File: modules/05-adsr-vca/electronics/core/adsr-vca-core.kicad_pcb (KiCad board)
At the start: 2 copper layers, 58 x 65 mm, 67 parts, among them J2 Conn_02x03_Odd_Even, J3 Conn_02x03_Odd_Even, J4 Conn_02x06_Odd_Even, J5 Conn_02x03_Odd_Even, J6 Conn_01x02, J7 Conn_02x05_Odd_Even, J8 Conn_02x03_Odd_Even, Q1 BC857, Q3 BC847BS, U1 LM324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

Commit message: ADSR+VCA JLCPCB verified for v1.0
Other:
- board text added: "SHMØERGH MODULEUR"
- board text added: "SM-05 ADSR VCA V1.0 / 2025 DEC"
- board text removed: "HM-05 ADSR VCA V0.2 / 2025 Aug"
- board text removed: "SHMØERGH HOG MODULEUR"

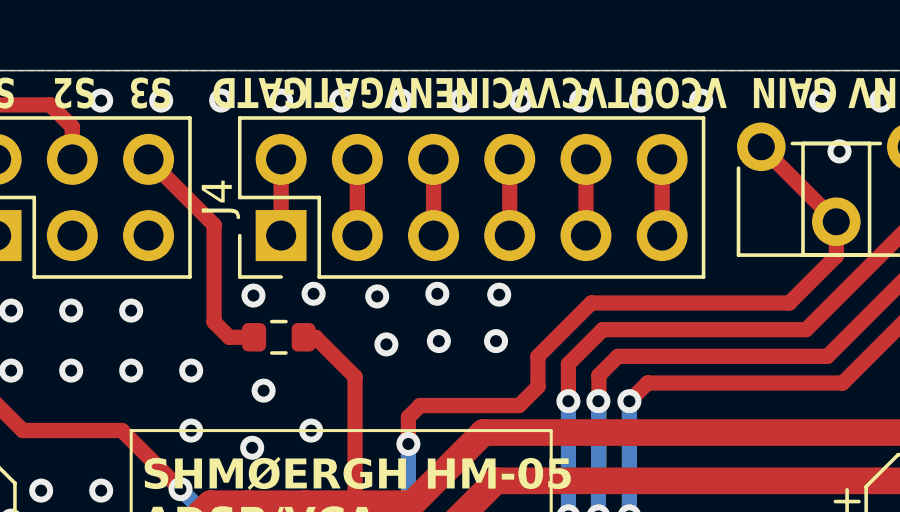
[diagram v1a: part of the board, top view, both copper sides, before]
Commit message: Fixed ADSR default connector
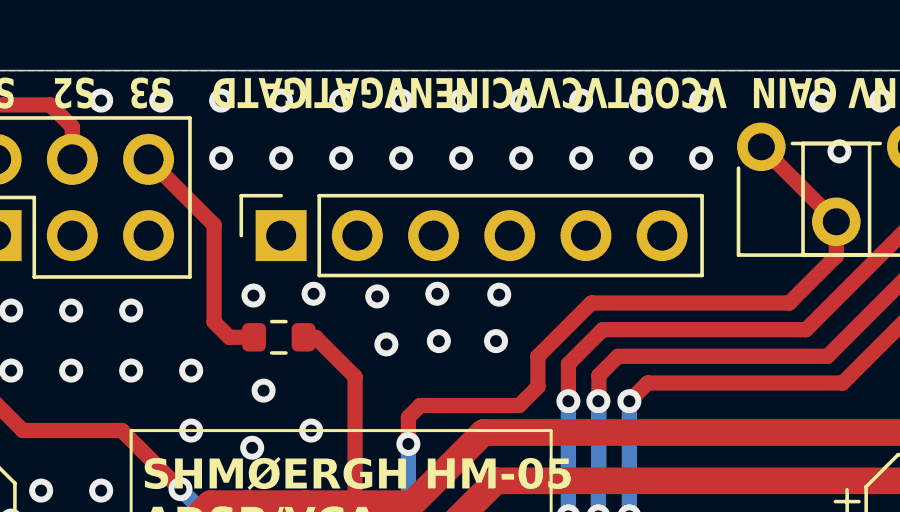
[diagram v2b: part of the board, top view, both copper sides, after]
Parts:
- J4: value Conn_02x06_Odd_Even -> Conn_01x06; footprint Connector_PinHeader_2.54mm:PinHeader_2x06_P2.54mm_Vertical -> Connector_PinSocket_2.54mm:PinSocket_1x06_P2.54mm_Vertical
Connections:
- J4 pad 1: Net-(J4-Pin_1) -> unconnected-(J4-Pin_1-Pad1)
- J4 pad 2: Net-(J4-Pin_1) -> unconnected-(J4-Pin_2-Pad2)
- J4 pad 3: Net-(J4-Pin_3) -> unconnected-(J4-Pin_3-Pad3)
- J4 pad 4: Net-(J4-Pin_3) -> unconnected-(J4-Pin_4-Pad4)
- J4 pad 5: Net-(J4-Pin_5) -> unconnected-(J4-Pin_5-Pad5)
- J4 pad 6: Net-(J4-Pin_5) -> unconnected-(J4-Pin_6-Pad6)
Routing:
- net Net-(J4-Pin_7): track 2.54 -> 0.00 mm
- net Net-(J4-Pin_5): track 2.54 -> 0.00 mm
- net Net-(J4-Pin_3): track 2.54 -> 0.00 mm
- net Net-(J4-Pin_11): track 2.54 -> 0.00 mm
- net Net-(J4-Pin_10): track 2.54 -> 0.00 mm
- net Net-(J4-Pin_1): track 2.54 -> 0.00 mm
- net GND: vias 330 -> 339
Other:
- board text added: "DEFAULTS"

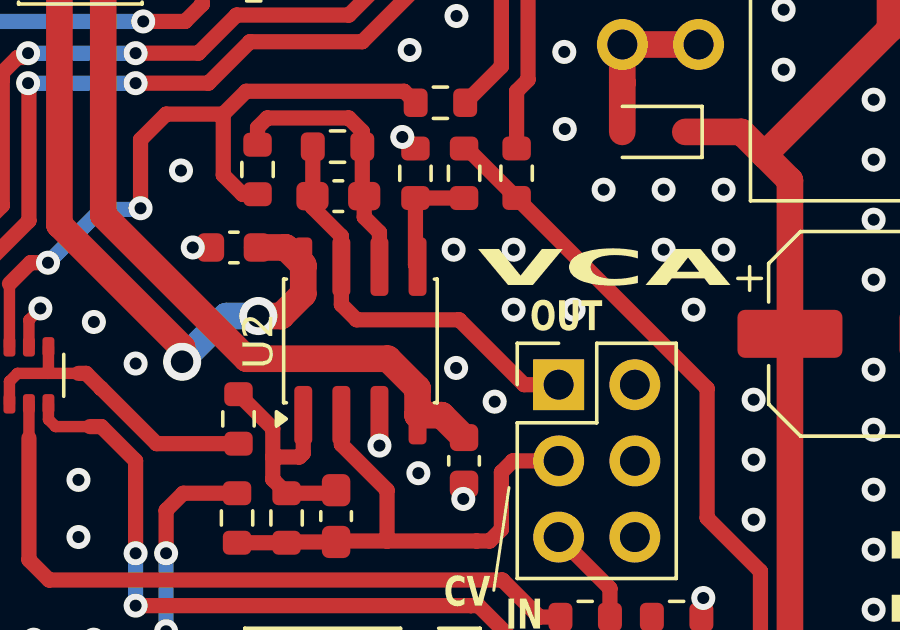
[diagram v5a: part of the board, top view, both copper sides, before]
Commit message: Added output resistor for VCA
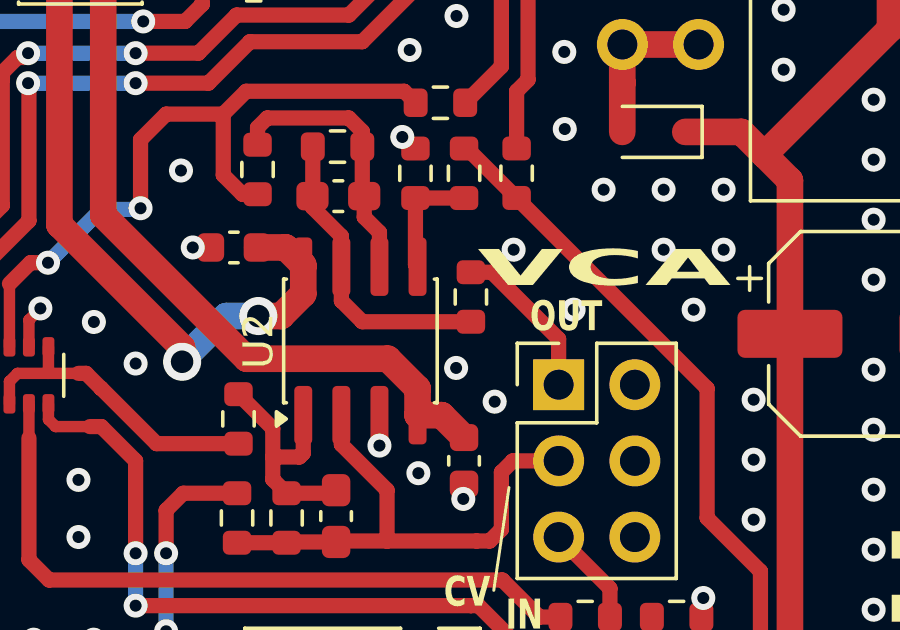
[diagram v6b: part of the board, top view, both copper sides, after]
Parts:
- added R15: 1k, Resistor_SMD:R_0603_1608Metric, F.Cu at (152.6, 88.6)
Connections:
- C8 pad 2: VCA_OUT -> Net-(C8-Pad2)
- R28 pad 2: VCA_OUT -> Net-(C8-Pad2)
- U2 pad 7: VCA_OUT -> Net-(C8-Pad2)
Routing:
- net Net-(C8-Pad2): track 0.00 -> 10.2 mm
- net VCA_OUT: track 14.0 -> 5.37 mm
- net GND: vias 339 -> 337

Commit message: Bumped rev of ADSR+VCA core board
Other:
- board text added: "SHMØERGH HM-05 ADSR/VCA core v1.2 2026 FEB"
- board text removed: "SHMØERGH HM-05 ADSR/VCA core v0.2 2025.OCT"
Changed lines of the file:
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@@
 		)
 	)
-	(gr_text "SHMØERGH HM-05 \nADSR/VCA core\nv0.2 2025.OCT"
+	(gr_text "SHMØERGH HM-05 \nADSR/VCA core\nv1.2 2026 FEB"
 		(at 138.351 61.272 0)
 		(layer "F.SilkS")
@@
 			(justify left bottom)
 		)
-		(render_cache "SHMØERGH HM-05 \nADSR/VCA core\nv0.2 2025.OCT" 0
+		(render_cache "SHMØERGH HM-05 \nADSR/VCA core\nv1.2 2026 FEB" 0
 			(polygon
 				(pts
@@
 			(polygon
 				(pts
-					(xy 139.368271 60.207216) (xy 139.368271 60.974749) (xy 139.499429 60.974749) (xy 139.499429 60.720187)
-					(xy 139.626741 60.720187) (xy 139.626741 60.589028) (xy 139.499429 60.589028) (xy 139.499429 60.207216)
-				)
-			)
-			(polygon
-				(pts
-					(xy 139.495521 60.970841) (xy 139.495521 61.102) (xy 139.881242 61.102) (xy 139.881242 60.970841)
-				)
-			)
-			(polygon
-				(pts
-					(xy 139.495521 60.079904) (xy 139.495521 60.211124) (xy 139.881242 60.211124) (xy 139.881242 60.079904)
-				)
-			)
-			(polygon
-				(pts
-					(xy 139.877334 60.207216) (xy 139.877334 60.334466) (xy 139.750084 60.334466) (xy 139.750084 60.465686)
-					(xy 139.877334 60.465686) (xy 139.877334 60.974749) (xy 140.008554 60.974749) (xy 140.008554 60.207216)
-				)
-			)
-			(polygon
-				(pts
-					(xy 139.622833 60.461778) (xy 139.622833 60.592936) (xy 139.753991 60.592936) (xy 139.753991 60.461778)
+					(xy 139.622833 60.338374) (xy 139.622833 60.970841) (xy 139.368271 60.970841) (xy 139.368271 61.102)
+					(xy 140.008554 61.102) (xy 140.008554 60.970841) (xy 139.753991 60.970841) (xy 139.753991 60.079904)
+					(xy 139.622833 60.079904) (xy 139.622833 60.207216) (xy 139.368271 60.207216) (xy 139.368271 60.338374)
 				)
 			)
@@
 			(polygon
 				(pts
-					(xy 145.598418 60.079904) (xy 145.598418 60.592936) (xy 146.111389 60.592936) (xy 146.111389 60.461778)
-					(xy 145.729576 60.461778) (xy 145.729576 60.211124) (xy 146.2387 60.211124) (xy 146.2387 60.079904)
+					(xy 145.725668 60.079904) (xy 145.725668 60.211124) (xy 146.111389 60.211124) (xy 146.111389 60.079904)
+				)
+			)
+			(polygon
+				(pts
+					(xy 145.598418 60.207216) (xy 145.598418 60.974749) (xy 145.729576 60.974749) (xy 145.729576 60.592936)
+					(xy 146.111389 60.592936) (xy 146.111389 60.461778) (xy 145.729576 60.461778) (xy 145.729576 60.207216)
 				)
 			)
@@
 			(polygon
 				(pts
-					(xy 146.111389 60.970841) (xy 145.725668 60.970841) (xy 145.725668 61.102) (xy 146.111389 61.102)
-				)
-			)
-			(polygon
-				(pts
-					(xy 145.729576 60.974749) (xy 145.729576 60.843591) (xy 145.598418 60.843591) (xy 145.598418 60.974749)
-				)
-			)
-			(polygon
-				(pts
-					(xy 146.743001 60.843591) (xy 146.743001 61.102) (xy 146.874159 61.102) (xy 146.874159 60.843591)
-				)
-			)
-			(polygon
-				(pts
-					(xy 147.378459 60.207216) (xy 147.378459 60.974749) (xy 147.509618 60.974749) (xy 147.509618 60.207216)
-				)
-			)
-			(polygon
-				(pts
-					(xy 147.50571 60.970841) (xy 147.50571 61.102) (xy 147.89143 61.102) (xy 147.89143 60.970841)
-				)
-			)
-			(polygon
-				(pts
-					(xy 147.887523 60.207216) (xy 147.887523 60.974749) (xy 148.018742 60.974749) (xy 148.018742 60.207216)
-				)
-			)
-			(polygon
-				(pts
-					(xy 147.50571 60.079904) (xy 147.50571 60.211124) (xy 147.89143 60.211124) (xy 147.89143 60.079904)
-				)
-			)
-			(polygon
-				(pts
-					(xy 148.26848 60.207216) (xy 148.26848 60.974749) (xy 148.399639 60.974749) (xy 148.399639 60.207216)
-				)
-			)
-			(polygon
-				(pts
-					(xy 148.395731 60.970841) (xy 148.395731 61.102) (xy 148.781451 61.102) (xy 148.781451 60.970841)
-				)
-			)
-			(polygon
-				(pts
-					(xy 148.777543 60.843591) (xy 148.777543 60.974749) (xy 148.908763 60.974749) (xy 148.908763 60.843591)
-				)
-			)
-			(polygon
-				(pts
-					(xy 148.395731 60.079904) (xy 148.395731 60.211124) (xy 148.781451 60.211124) (xy 148.781451 60.079904)
-				)
-			)
-			(polygon
-				(pts
-					(xy 148.777543 60.207216) (xy 148.777543 60.338374) (xy 148.908763 60.338374) (xy 148.908763 60.207216)
-				)
-			)
-			(polygon
-				(pts
-					(xy 149.158501 60.079904) (xy 149.158501 60.211124) (xy 149.413063 60.211124) (xy 149.413063 61.102)
-					(xy 149.544222 61.102) (xy 149.544222 60.211124) (xy 149.798784 60.211124) (xy 149.798784 60.079904)
-				)
-			)
+					(xy 145.725668 60.970841) (xy 145.725668 61.102) (xy 146.111389 61.102) (xy 146.111389 60.970841)
+				)
+			)
+			(polygon
+				(pts
+					(xy 146.107481 60.207216) (xy 146.107481 60.338374) (xy 146.2387 60.338374) (xy 146.2387 60.207216)
+				)
+			)
+			(polygon
+				(pts
+					(xy 147.378459 60.079904) (xy 147.378459 61.102) (xy 147.509618 61.102) (xy 147.509618 60.592936)
+					(xy 147.89143 60.592936) (xy 147.89143 60.461778) (xy 147.509618 60.461778) (xy 147.509618 60.211124)
+					(xy 148.018742 60.211124) (xy 148.018742 60.079904)
+				)
+			)
+			(polygon
+				(pts
+					(xy 148.26848 60.079904) (xy 148.26848 61.102) (xy 148.908763 61.102) (xy 148.908763 60.970841)
+					(xy 148.399639 60.970841) (xy 148.399639 60.592936) (xy 148.781451 60.592936) (xy 148.781451 60.461778)
+					(xy 148.399639 60.461778) (xy 148.399639 60.211124) (xy 148.908763 60.211124) (xy 148.908763 60.079904)
+				)
+			)
+			(polygon
+				(pts
+					(xy 149.158501 60.079904) (xy 149.158501 61.102) (xy 149.671472 61.102) (xy 149.671472 60.970841)
+					(xy 149.28966 60.970841) (xy 149.28966 60.592936) (xy 149.671472 60.592936) (xy 149.671472 60.461778)
+					(xy 149.28966 60.461778) (xy 149.28966 60.211124) (xy 149.671472 60.211124) (xy 149.671472 60.079904)
+				)
+			)
+			(polygon
+				(pts
+					(xy 149.667564 60.589028) (xy 149.667564 60.974749) (xy 149.798784 60.974749) (xy 149.798784 60.589028)
+				)
+			)
+			(polygon
+				(pts
+					(xy 149.667564 60.207216) (xy 149.667564 60.465686) (xy 149.798784 60.465686) (xy 149.798784 60.207216)
+				)
+			)

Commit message: KiCAD version update - ADSR+VCA
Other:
- board text added: "SHMØERGH HM-05 ADSR/VCA core v1.2"
- board text removed: "SHMØERGH HM-05 ADSR/VCA core v1.2 2026 FEB"
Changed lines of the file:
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@@
 		)
 	)
-	(gr_text "SHMØERGH HM-05 \nADSR/VCA core\nv1.2 2026 FEB"
+	(gr_text "SHMØERGH HM-05 \nADSR/VCA core\nv1.2"
 		(at 138.351 61.272 0)
 		(layer "F.SilkS")
@@
 			(justify left bottom)
 		)
-		(render_cache "SHMØERGH HM-05 \nADSR/VCA core\nv1.2 2026 FEB" 0
+		(render_cache "SHMØERGH HM-05 \nADSR/VCA core\nv1.2" 0
 			(polygon
 				(pts
@@
 				)
 			)
-			(polygon
-				(pts
-					(xy 142.928355 60.843591) (xy 142.928355 61.102) (xy 143.568637 61.102) (xy 143.568637 60.970841)
-					(xy 143.059513 60.970841) (xy 143.059513 60.843591)
-				)
-			)
-			(polygon
-				(pts
-					(xy 143.441326 60.211124) (xy 143.441326 60.079904) (xy 143.055605 60.079904) (xy 143.055605 60.211124)
-				)
-			)
-			(polygon
-				(pts
-					(xy 143.437418 60.207216) (xy 143.437418 60.465686) (xy 143.568637 60.465686) (xy 143.568637 60.207216)
-				)
-			)
-			(polygon
-				(pts
-					(xy 143.055605 60.716279) (xy 143.055605 60.847498) (xy 143.186825 60.847498) (xy 143.186825 60.716279)
-				)
-			)
-			(polygon
-				(pts
-					(xy 142.928355 60.207216) (xy 142.928355 60.338374) (xy 143.059513 60.338374) (xy 143.059513 60.207216)
-				)
-			)
-			(polygon
-				(pts
-					(xy 143.310167 60.461778) (xy 143.310167 60.592936) (xy 143.441326 60.592936) (xy 143.441326 60.461778)
-				)
-			)
-			(polygon
-				(pts
-					(xy 143.182917 60.589028) (xy 143.182917 60.720187) (xy 143.314075 60.720187) (xy 143.314075 60.589028)
-				)
-			)
-			(polygon
-				(pts
-					(xy 143.818376 60.207216) (xy 143.818376 60.974749) (xy 143.949534 60.974749) (xy 143.949534 60.720187)
-					(xy 144.076846 60.720187) (xy 144.076846 60.589028) (xy 143.949534 60.589028) (xy 143.949534 60.207216)
-				)
-			)
-			(polygon
-				(pts
-					(xy 143.945626 60.970841) (xy 143.945626 61.102) (xy 144.331347 61.102) (xy 144.331347 60.970841)
-				)
-			)
-			(polygon
-				(pts
-					(xy 143.945626 60.079904) (xy 143.945626 60.211124) (xy 144.331347 60.211124) (xy 144.331347 60.079904)
-				)
-			)
-			(polygon
-				(pts
-					(xy 144.327439 60.207216) (xy 144.327439 60.334466) (xy 144.200188 60.334466) (xy 144.200188 60.465686)
-					(xy 144.327439 60.465686) (xy 144.327439 60.974749) (xy 144.458658 60.974749) (xy 144.458658 60.207216)
-				)
-			)
-			(polygon
-				(pts
-					(xy 144.072938 60.461778) (xy 144.072938 60.592936) (xy 144.204096 60.592936) (xy 144.204096 60.461778)
-				)
-			)
-			(polygon
-				(pts
-					(xy 144.708397 60.843591) (xy 144.708397 61.102) (xy 145.348679 61.102) (xy 145.348679 60.970841)
-					(xy 144.839555 60.970841) (xy 144.839555 60.843591)
-				)
-			)
-			(polygon
-				(pts
-					(xy 145.221368 60.211124) (xy 145.221368 60.079904) (xy 144.835647 60.079904) (xy 144.835647 60.211124)
-				)
-			)
-			(polygon
-				(pts
-					(xy 145.21746 60.207216) (xy 145.21746 60.465686) (xy 145.348679 60.465686) (xy 145.348679 60.207216)
-				)
-			)
-			(polygon
-				(pts
-					(xy 144.835647 60.716279) (xy 144.835647 60.847498) (xy 144.966867 60.847498) (xy 144.966867 60.716279)
-				)
-			)
-			(polygon
-				(pts
-					(xy 144.708397 60.207216) (xy 144.708397 60.338374) (xy 144.839555 60.338374) (xy 144.839555 60.207216)
-				)
-			)
-			(polygon
-				(pts
-					(xy 145.090209 60.461778) (xy 145.090209 60.592936) (xy 145.221368 60.592936) (xy 145.221368 60.461778)
-				)
-			)
-			(polygon
-				(pts
-					(xy 144.962959 60.589028) (xy 144.962959 60.720187) (xy 145.094117 60.720187) (xy 145.094117 60.589028)
-				)
-			)
-			(polygon
-				(pts
-					(xy 145.725668 60.079904) (xy 145.725668 60.211124) (xy 146.111389 60.211124) (xy 146.111389 60.079904)
-				)
-			)
-			(polygon
-				(pts
-					(xy 145.598418 60.207216) (xy 145.598418 60.974749) (xy 145.729576 60.974749) (xy 145.729576 60.592936)
-					(xy 146.111389 60.592936) (xy 146.111389 60.461778) (xy 145.729576 60.461778) (xy 145.729576 60.207216)
-				)
-			)
-			(polygon
-				(pts
-					(xy 146.107481 60.589028) (xy 146.107481 60.974749) (xy 146.2387 60.974749) (xy 146.2387 60.589028)
-				)
-			)
-			(polygon
-				(pts
-					(xy 145.725668 60.970841) (xy 145.725668 61.102) (xy 146.111389 61.102) (xy 146.111389 60.970841)
-				)
-			)
-			(polygon
-				(pts
-					(xy 146.107481 60.207216) (xy 146.107481 60.338374) (xy 146.2387 60.338374) (xy 146.2387 60.207216)
-				)
-			)
-			(polygon
-				(pts
-					(xy 147.378459 60.079904) (xy 147.378459 61.102) (xy 147.509618 61.102) (xy 147.509618 60.592936)
-					(xy 147.89143 60.592936) (xy 147.89143 60.461778) (xy 147.509618 60.461778) (xy 147.509618 60.211124)
-					(xy 148.018742 60.211124) (xy 148.018742 60.079904)
-				)
-			)
-			(polygon
-				(pts
-					(xy 148.26848 60.079904) (xy 148.26848 61.102) (xy 148.908763 61.102) (xy 148.908763 60.970841)
-					(xy 148.399639 60.970841) (xy 148.399639 60.592936) (xy 148.781451 60.592936) (xy 148.781451 60.461778)
-					(xy 148.399639 60.461778) (xy 148.399639 60.211124) (xy 148.908763 60.211124) (xy 148.908763 60.079904)
-				)
-			)
-			(polygon
-				(pts
-					(xy 149.158501 60.079904) (xy 149.158501 61.102) (xy 149.671472 61.102) (xy 149.671472 60.970841)
-					(xy 149.28966 60.970841) (xy 149.28966 60.592936) (xy 149.671472 60.592936) (xy 149.671472 60.461778)
-					(xy 149.28966 60.461778) (xy 149.28966 60.211124) (xy 149.671472 60.211124) (xy 149.671472 60.079904)
-				)
-			)
-			(polygon
-				(pts
-					(xy 149.667564 60.589028) (xy 149.667564 60.974749) (xy 149.798784 60.974749) (xy 149.798784 60.589028)
-				)
-			)
-			(polygon
-				(pts
-					(xy 149.667564 60.207216) (xy 149.667564 60.465686) (xy 149.798784 60.465686) (xy 149.798784 60.207216)
-				)
-			)
